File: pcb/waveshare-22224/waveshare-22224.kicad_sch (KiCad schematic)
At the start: 4 parts, among them J2 Conn_01x08_Socket

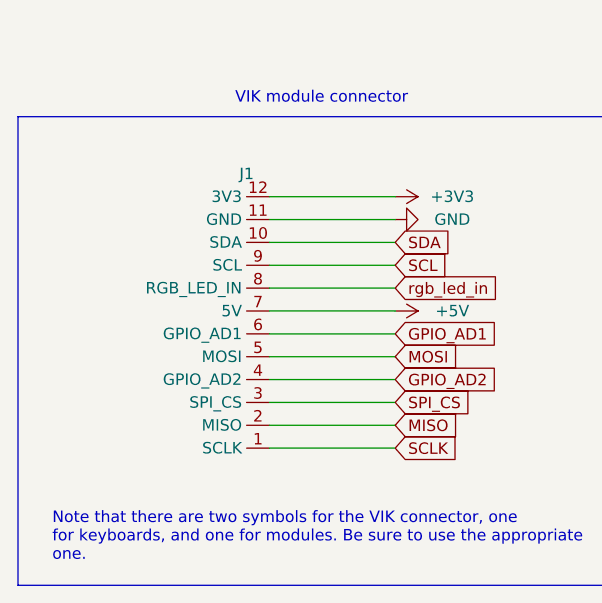
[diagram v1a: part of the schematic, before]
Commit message: updated vikm connector symbols, per some recommendations from sigprof in fingerpunch discord
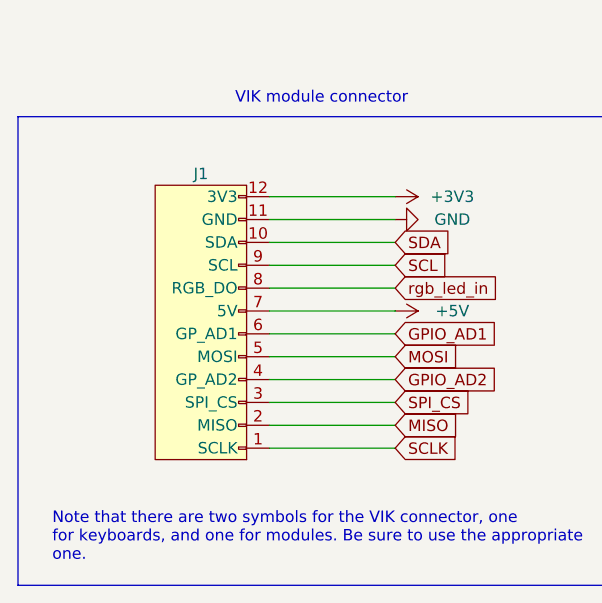
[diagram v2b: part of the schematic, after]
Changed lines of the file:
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@@
     )
   )
-  (symbol (lib_id "vik:vik-module-connector") (at 81.28 72.39 180) (unit 1)
-    (in_bom yes) (on_board yes) (dnp no) (fields_autoplaced)
-    (property "Reference" "J1" (at 78.74 55.88 0)
+  (symbol (lib_id "vik:vik-module-connector") (at 73.66 73.66 180) (unit 1)
+    (in_bom yes) (on_board yes) (dnp no)
+    (property "Reference" "J1" (at 73.66 55.88 0)
       (effects (font (size 1.27 1.27)))
     )
-    (property "Value" "~" (at 81.28 78.74 0)
+    (property "Value" "~" (at 73.66 80.01 0)
       (effects (font (size 1.27 1.27)))
     )
-    (property "Footprint" "vik:vik-module-connector-horizontal" (at 81.28 78.74 0)
+    (property "Footprint" "vik:vik-module-connector-horizontal" (at 73.66 80.01 0)
       (effects (font (size 1.27 1.27)) hide)
     )
-    (property "Datasheet" "" (at 81.28 78.74 0)
+    (property "Datasheet" "" (at 73.66 80.01 0)
       (effects (font (size 1.27 1.27)) hide)
     )
-    (property "LCSC" "C479750" (at 81.28 72.39 0)
+    (property "LCSC" "C479750" (at 73.66 73.66 0)
       (effects (font (size 1.27 1.27)) hide)
     )
